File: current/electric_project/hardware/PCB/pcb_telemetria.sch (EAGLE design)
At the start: 42 parts

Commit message: Schematic e code conforming
The mux pins in the code are now updated (EN on the ground rsrs) and the circuit project are already routed with the new mux pins
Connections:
- removed net GND1: U$1.GND1
- net 13: now also HC4067.S2
- net 14: now also HC4067.S1
- net 33: no longer HC4067.EN
- net 34: no longer HC4067.S2
- net 35: no longer HC4067.S1
- net GND: now also HC4067.EN, U$1.GND1
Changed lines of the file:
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@@
 <?xml version="1.0" encoding="utf-8"?>
 <!DOCTYPE eagle SYSTEM "eagle.dtd">
-<eagle version="9.4.2">
+<eagle version="9.5.0">
 <drawing>
 <settings>
@@
 <label x="-50.292" y="127.762" size="1.778" layer="95"/>
 </segment>
-<segment>
-<pinref part="HC4067" gate="G$1" pin="EN"/>
-<wire x1="40.132" y1="150.622" x2="40.132" y2="160.782" width="0.1524" layer="91"/>
-<label x="39.878" y="158.242" size="1.778" layer="95" rot="R90"/>
-</segment>
 </net>
 <net name="25" class="0">
@@
 <label x="-50.292" y="122.682" size="1.778" layer="95"/>
 </segment>
+<segment>
+<pinref part="HC4067" gate="G$1" pin="S1"/>
+<wire x1="35.052" y1="150.622" x2="35.052" y2="160.782" width="0.1524" layer="91"/>
+<label x="34.798" y="158.496" size="1.778" layer="95" rot="R90"/>
+</segment>
 </net>
 <net name="13" class="0">
@@
 <wire x1="-40.132" y1="120.142" x2="-50.292" y2="120.142" width="0.1524" layer="91"/>
 <label x="-50.292" y="120.142" size="1.778" layer="95"/>
+</segment>
+<segment>
+<pinref part="HC4067" gate="G$1" pin="S2"/>
+<wire x1="32.512" y1="150.622" x2="32.512" y2="160.782" width="0.1524" layer="91"/>
+<label x="32.258" y="158.496" size="1.778" layer="95" rot="R90"/>
 </segment>
 </net>
@@
 <label x="-111.76" y="48.26" size="1.778" layer="95"/>
 </segment>
+<segment>
+<pinref part="HC4067" gate="G$1" pin="EN"/>
+<wire x1="40.132" y1="150.622" x2="40.132" y2="160.782" width="0.1524" layer="91"/>
+<label x="39.878" y="156.21" size="1.778" layer="95" rot="R90"/>
+</segment>
+<segment>
+<pinref part="U$1" gate="G$1" pin="GND1"/>
+<wire x1="-7.112" y1="125.222" x2="6.096" y2="125.222" width="0.1524" layer="91"/>
+<label x="0.762" y="125.476" size="1.778" layer="95"/>
+</segment>
 </net>
 <net name="22" class="0">
@@
 <label x="-50.292" y="135.382" size="1.778" layer="95"/>
 </segment>
-<segment>
-<pinref part="HC4067" gate="G$1" pin="S2"/>
-<wire x1="32.512" y1="150.622" x2="32.512" y2="160.782" width="0.1524" layer="91"/>
-<label x="32.512" y="160.782" size="1.778" layer="95" rot="R90" align="bottom-right"/>
-</segment>
 </net>
 <net name="35" class="0">
@@
 <label x="-50.292" y="132.842" size="1.778" layer="95"/>
 </segment>
-<segment>
-<pinref part="HC4067" gate="G$1" pin="S1"/>
-<wire x1="35.052" y1="150.622" x2="35.052" y2="160.782" width="0.1524" layer="91"/>
-<label x="35.052" y="160.782" size="1.778" layer="95" rot="R90" align="bottom-right"/>
-</segment>
 </net>
 <net name="32" class="0">
@@
 <pinref part="HC4067" gate="G$1" pin="S0"/>
 <wire x1="37.592" y1="150.622" x2="37.592" y2="160.782" width="0.1524" layer="91"/>
-<label x="37.592" y="160.782" size="1.778" layer="95" rot="R90" align="bottom-right"/>
+<label x="37.338" y="158.242" size="1.778" layer="95" rot="R90"/>
 </segment>
 </net>
@@
 </segment>
 </net>
-<net name="GND1" class="0">
-<segment>
-<pinref part="U$1" gate="G$1" pin="GND1"/>
-<wire x1="-7.112" y1="125.222" x2="5.588" y2="125.222" width="0.1524" layer="91"/>
-<label x="6.096" y="125.476" size="1.778" layer="95" align="bottom-right"/>
-</segment>
-</net>

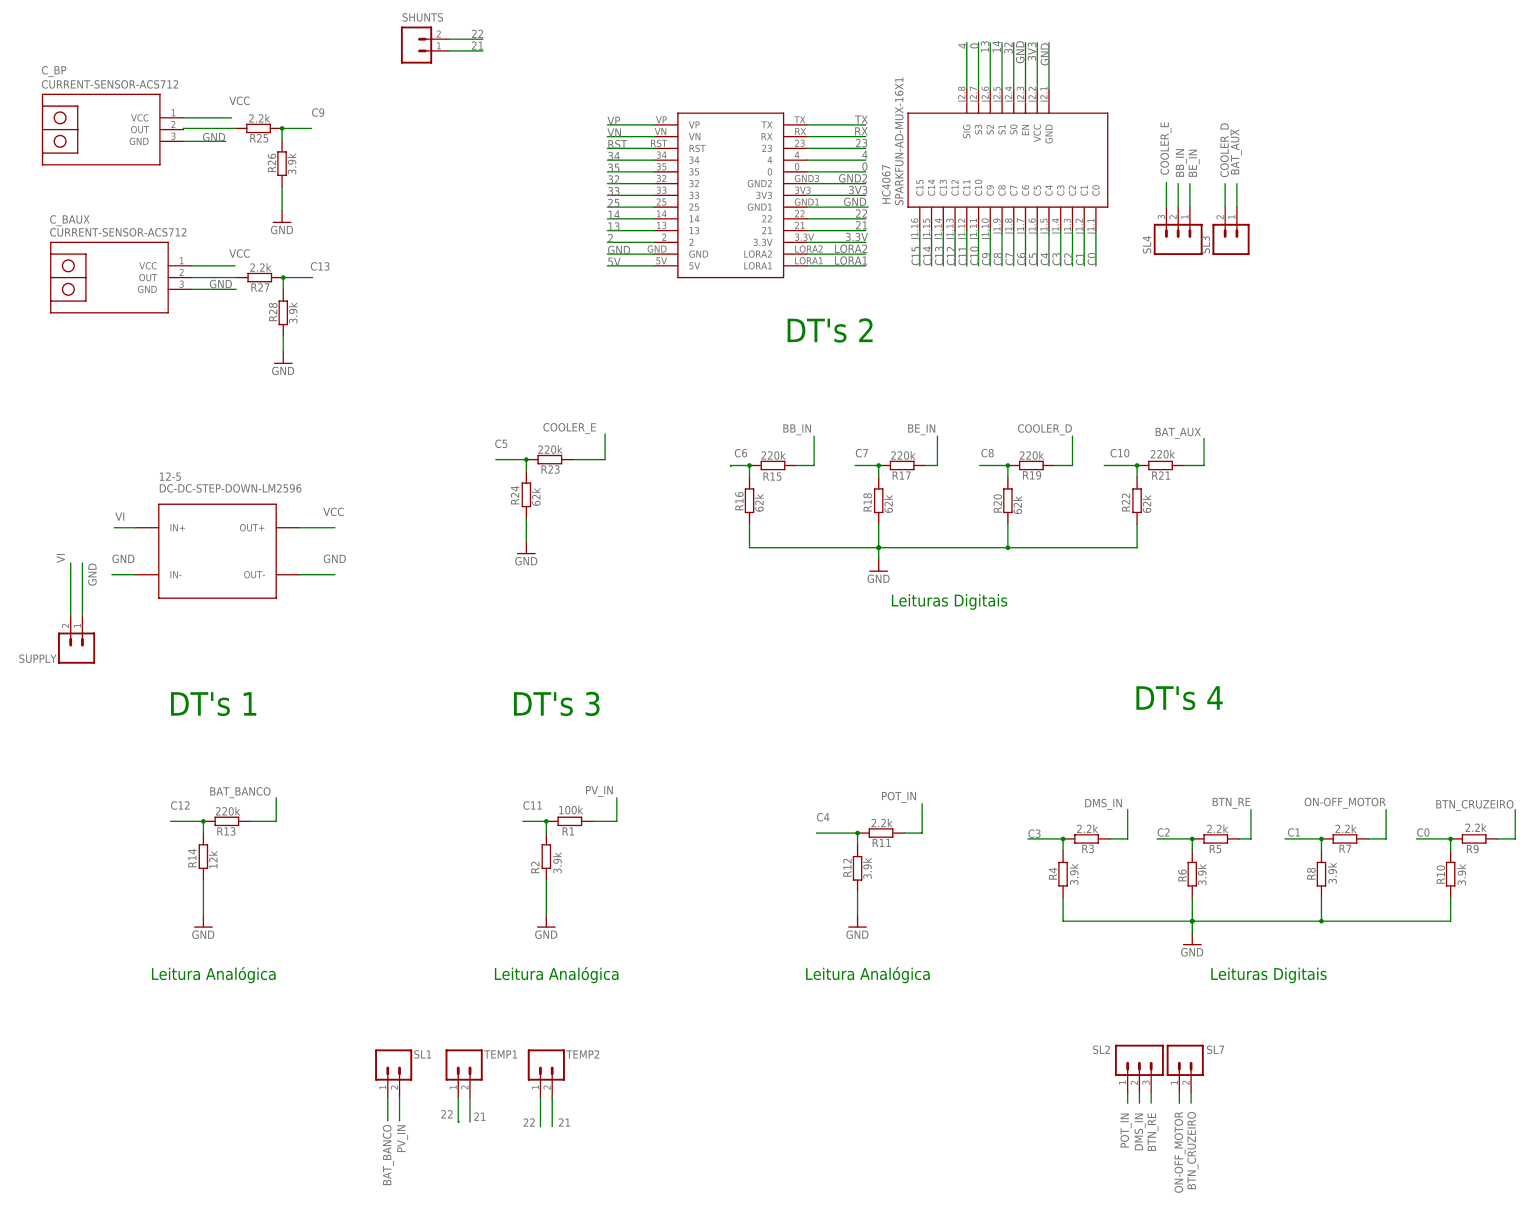
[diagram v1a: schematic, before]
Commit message: mudancas na placa
resistores atualizados com sucesso

Co-Authored-By: Raquel Perim <raquelperim@users.noreply.github.com>
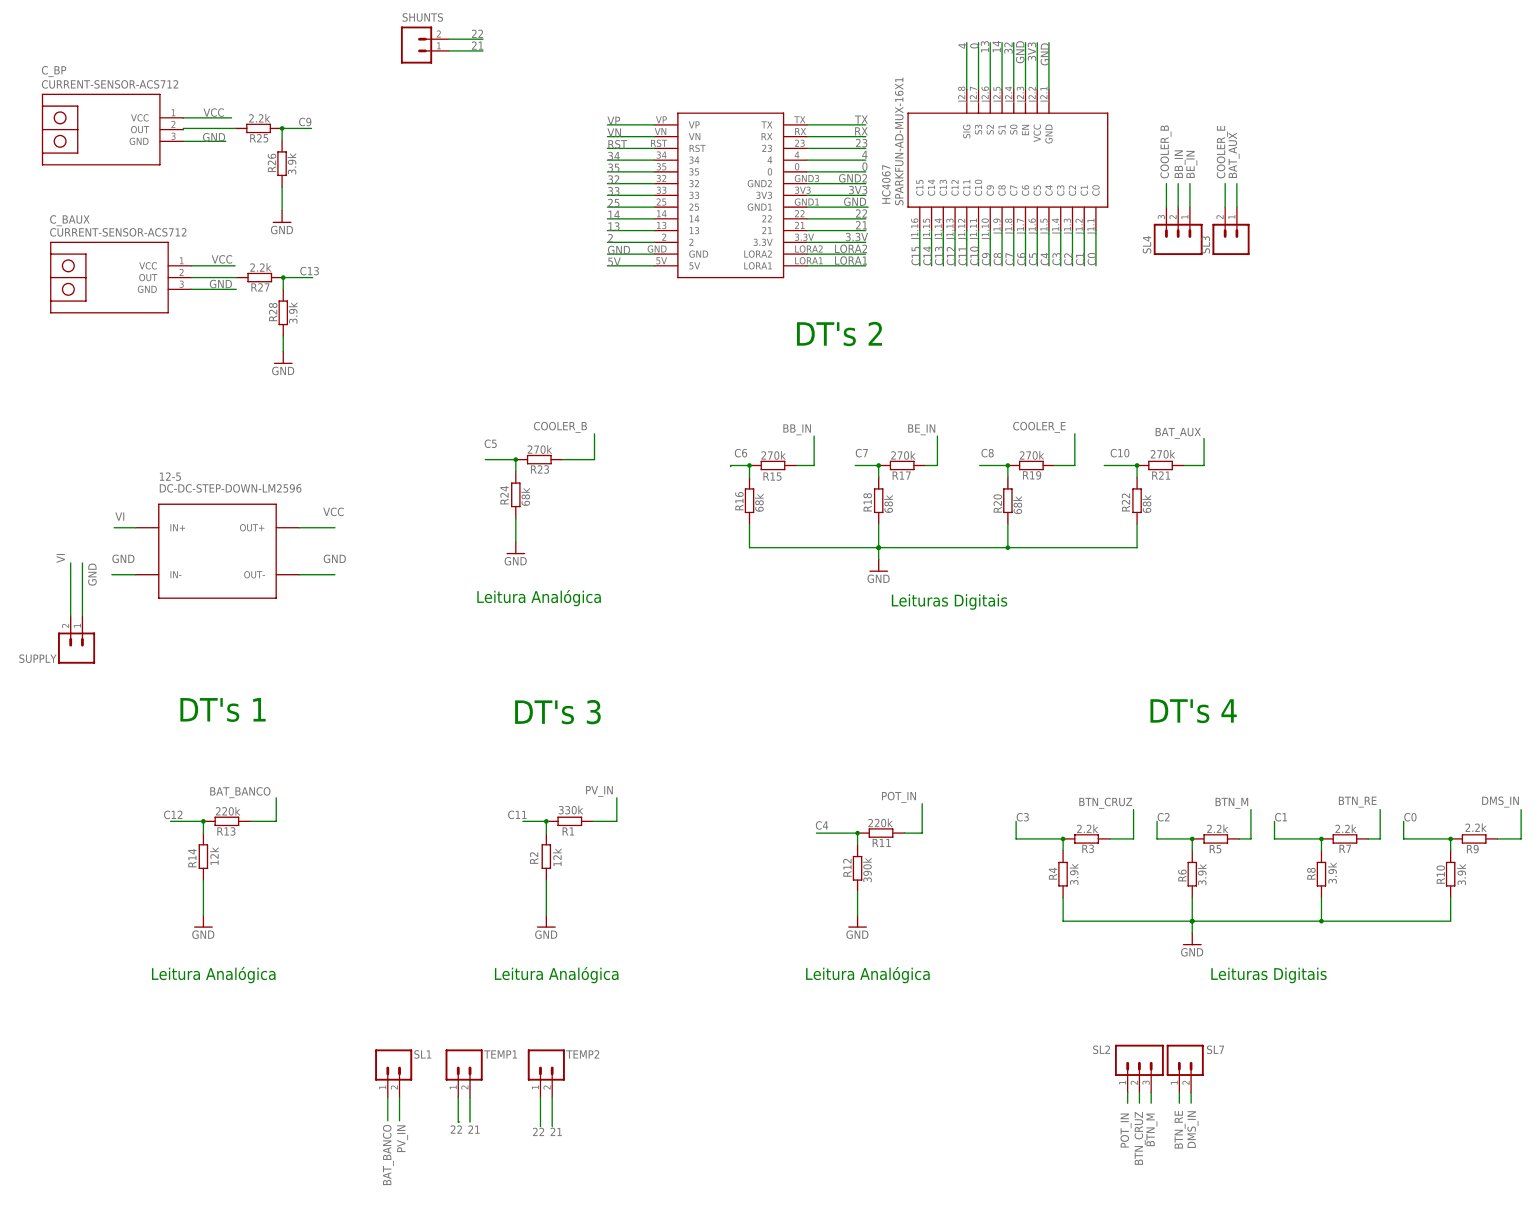
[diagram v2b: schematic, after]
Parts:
- R1: value 100k -> 330k
- R11: value 2.2k -> 220k
- R12: value 3.9k -> 390k
- R15, R17, R19, R21, R23: value 220k -> 270k
- R16, R18, R20, R22, R24: value 62k -> 68k
- R2: value 3.9k -> 12k
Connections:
- removed net BTN_CRUZEIRO: R9.2, SL7.2
- removed net COOLER_D: R19.1, SL3.2
- removed net ON-OFF_MOTOR: R7.1, SL7.1
- new net BTN_CRUZ: R3.1, SL2.2
- new net BTN_M: R5.2, SL2.3
- new net COOLER_B: R23.1, SL4.3
- net BTN_RE: now also R7.1, SL7.1; no longer R5.2, SL2.3
- net COOLER_E: now also R19.1, SL3.2; no longer R23.1, SL4.3
- net DMS_IN: now also R9.2, SL7.2; no longer R3.1, SL2.2
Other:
- moved on the sheet: R23, R24
